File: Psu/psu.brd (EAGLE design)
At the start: 77.5 x 91.4 mm, 34 parts, among them Q1 FDPF18N50T, Q2 FDPF18N50T, Q3 FDPF18N50T, Q4 FDPF18N50T, X1 MOUNT-PAD2.0, X2 MOUNT-PAD2.0, X3 MOUNT-PAD2.0, X4 MOUNT-PAD2.0, X5 MOUNT-PAD2.0

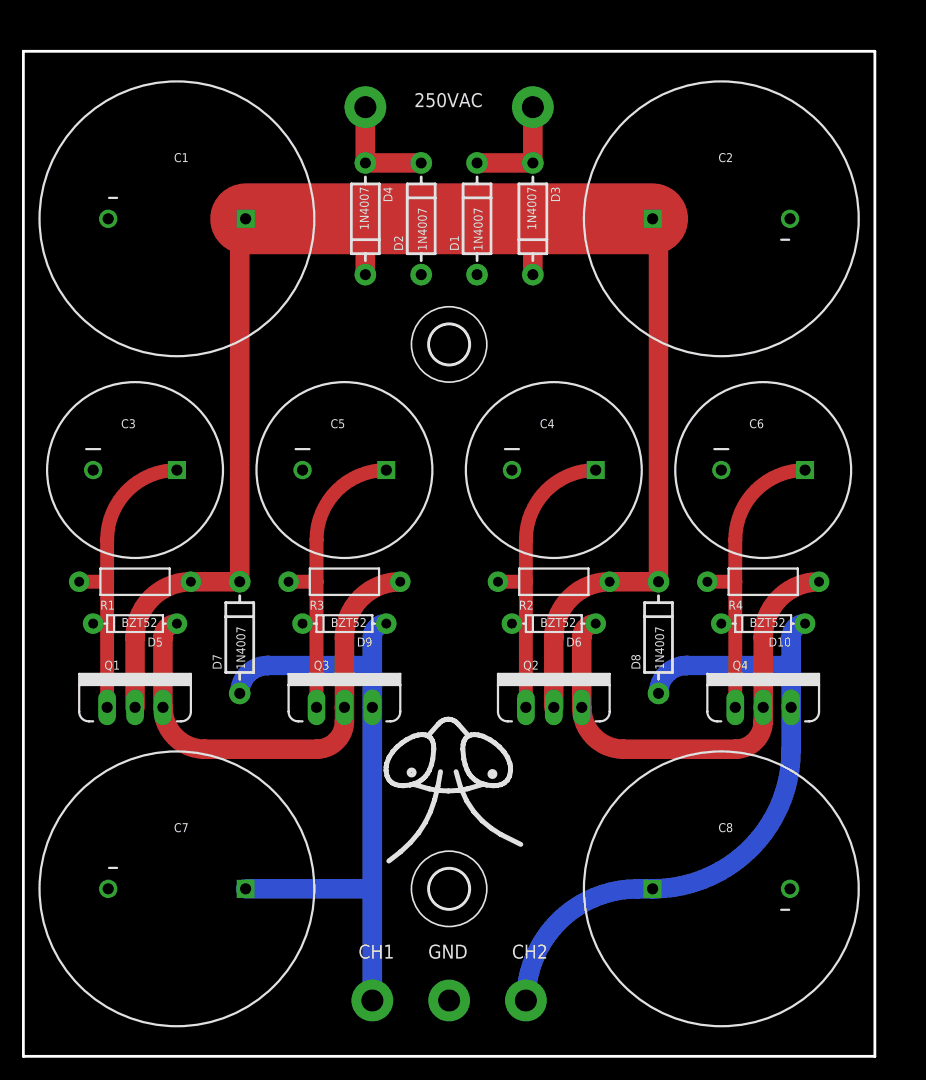
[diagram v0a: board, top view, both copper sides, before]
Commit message: More mounting holes
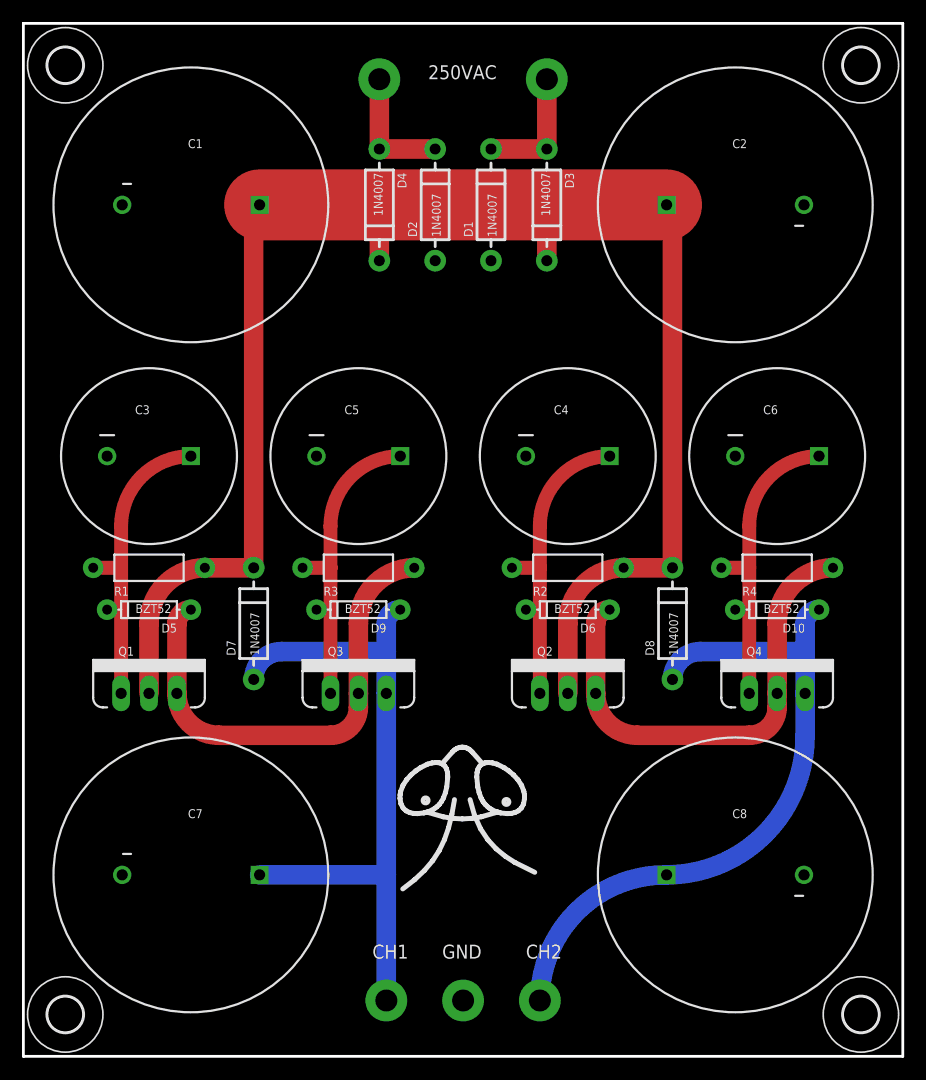
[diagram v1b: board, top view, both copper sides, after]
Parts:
- added H3, H4: MOUNT-HOLE3.2, holes:3,2
- H1, H2: value MOUNT-HOLE3.6 -> MOUNT-HOLE3.2; device holes:3,6 -> holes:3,2
- moved H1 45.3 mm to (76.2, 90.2)
- moved H2 36.7 mm to (3.81, 3.81)
- moved X1 2.84 mm to (47.6, 88.9)
- moved X2 2.84 mm to (32.4, 88.9)
- moved LOGO1 2.84 mm to (40.0, 21.6)
- moved D6 1.80 mm to (49.5, 40.6)
- moved Q2 1.80 mm to (49.5, 33.0)
- moved R2 1.80 mm to (49.5, 44.5)
- moved D5 1.80 mm to (11.4, 40.6)
- moved D9 1.80 mm to (30.5, 40.6)
- moved Q1 1.80 mm to (11.4, 33.0)
- moved Q3 1.80 mm to (30.5, 33.0)
- moved R1 1.80 mm to (11.4, 44.5)
- moved R3 1.80 mm to (30.5, 44.5)
- moved C7 1.80 mm to (15.2, 16.5)
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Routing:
- net TR2: track 10.2 -> 11.4 mm
- net TR1: track 10.2 -> 11.4 mm
- net HT1: track 59.5 -> 60.7 mm
- net HT2: track 58.7 -> 59.3 mm
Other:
- board size 77.5 x 91.4 mm -> 80 x 94 mm
